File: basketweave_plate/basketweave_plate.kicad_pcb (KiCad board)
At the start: 2 copper layers, 371.5 x 119.1 mm, 1 part

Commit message: Modify plate logo for Basketweave-S and move it into PCB footprint library
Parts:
- G***: footprint basketweave_plate:logo_plate -> basketweave:logo_plate
- moved G*** 1.54 mm to (88.8, 130.1)
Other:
- board text added: "JLCJLCJLCJLC"

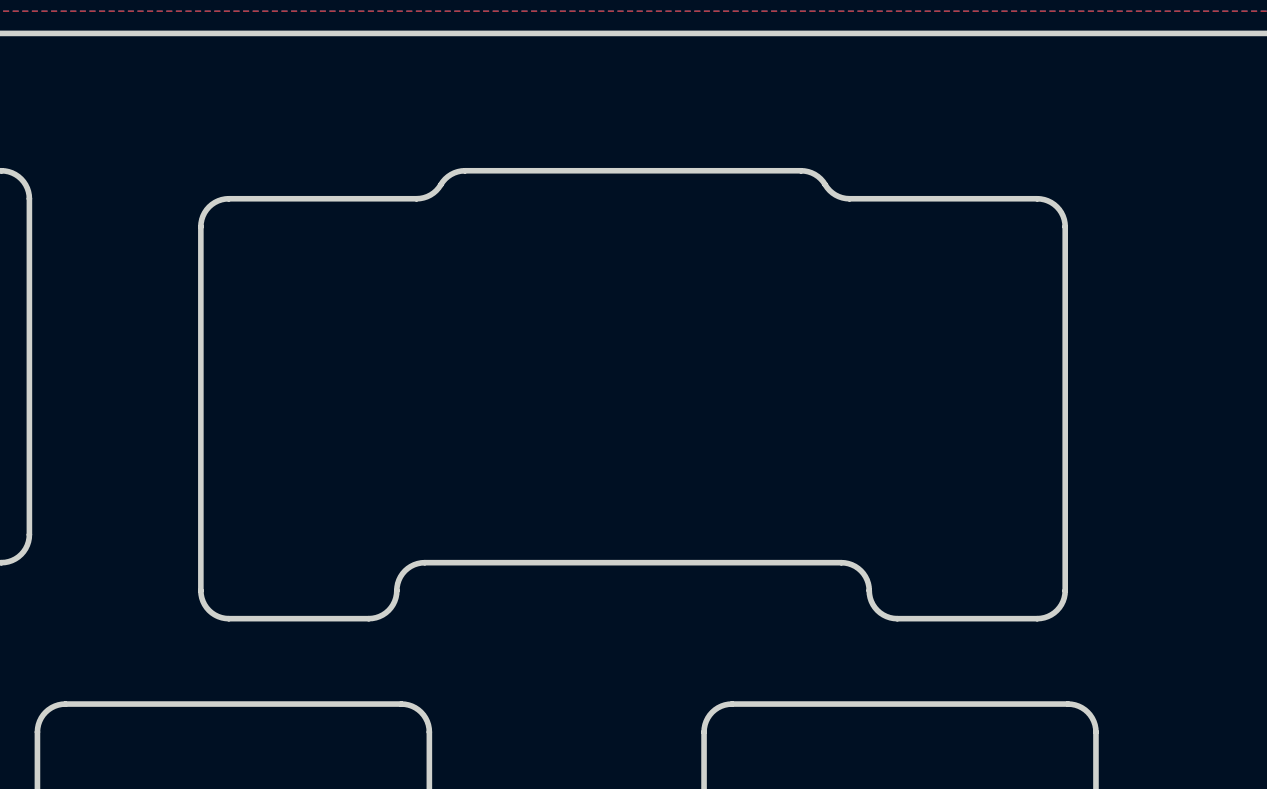
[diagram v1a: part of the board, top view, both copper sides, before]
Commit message: Add support for split backspace
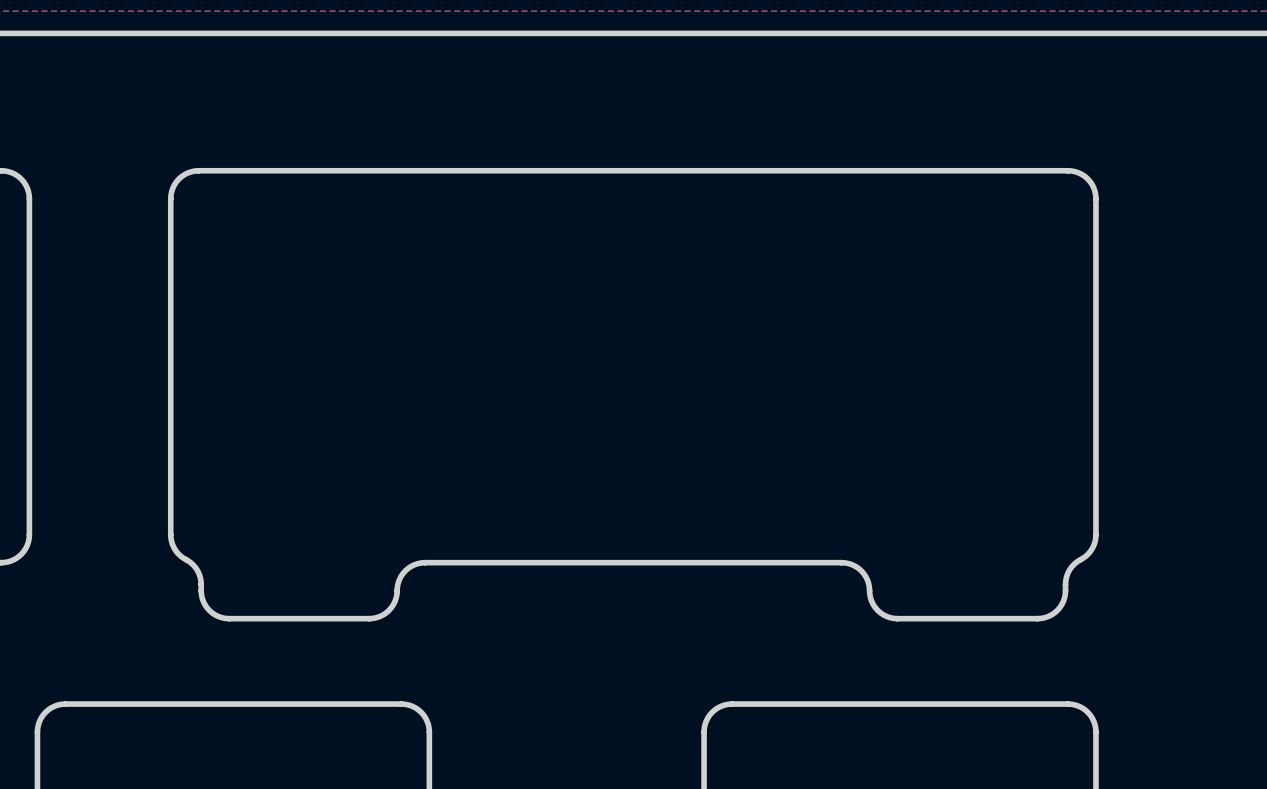
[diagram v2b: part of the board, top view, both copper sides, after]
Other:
- outline, holes or cut-outs redrawn

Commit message: Enlarge right space cutout; fix position according to PCB
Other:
- outline, holes or cut-outs redrawn
- net class Default removed
- board text removed: "JLCJLCJLCJLC"
